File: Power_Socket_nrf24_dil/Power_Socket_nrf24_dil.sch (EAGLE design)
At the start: 25 parts, among them IC1 REG1117, IC2 ATMEGA168-20P, K1 ZF112, T1 BC337

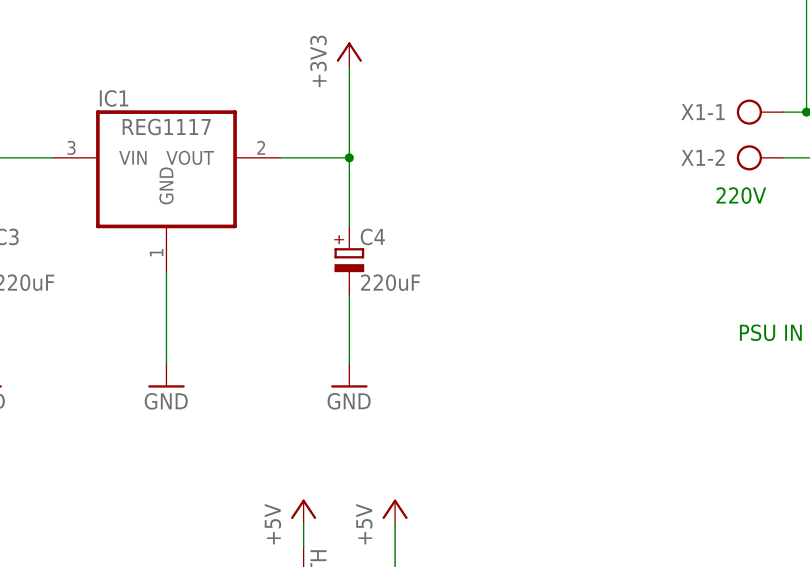
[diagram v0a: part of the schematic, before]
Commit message: Added Image Export of Eagle Files
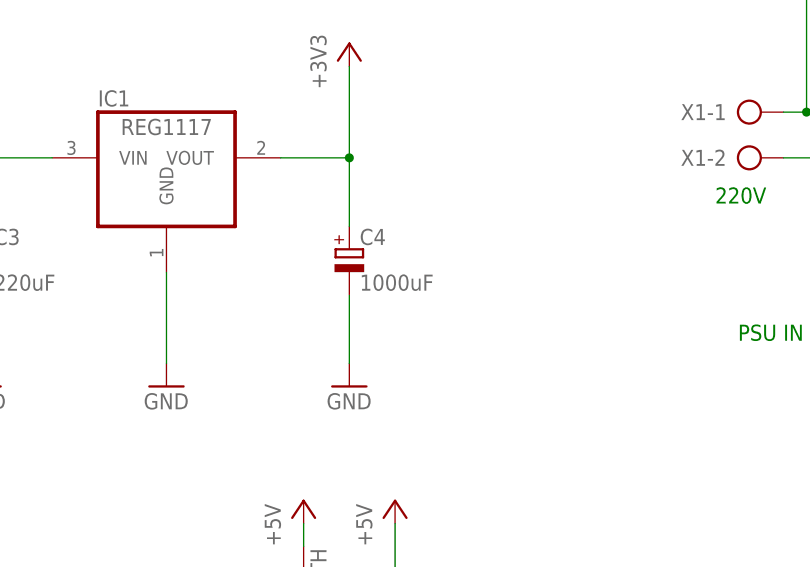
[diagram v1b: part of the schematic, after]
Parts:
- C4: value 220uF -> 1000uF
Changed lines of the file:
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@@
 <part name="+3V3" library="supply1" deviceset="+3V3" device=""/>
 <part name="C3" library="resistor" deviceset="CPOL-EU" device="E2.5-6" value="220uF"/>
-<part name="C4" library="resistor" deviceset="CPOL-EU" device="E2.5-6" value="220uF"/>
+<part name="C4" library="resistor" deviceset="CPOL-EU" device="E2.5-6" value="1000uF"/>
 <part name="GND9" library="supply1" deviceset="GND" device=""/>
 <part name="GND10" library="supply1" deviceset="GND" device=""/>
